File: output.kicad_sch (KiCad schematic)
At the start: 6 parts

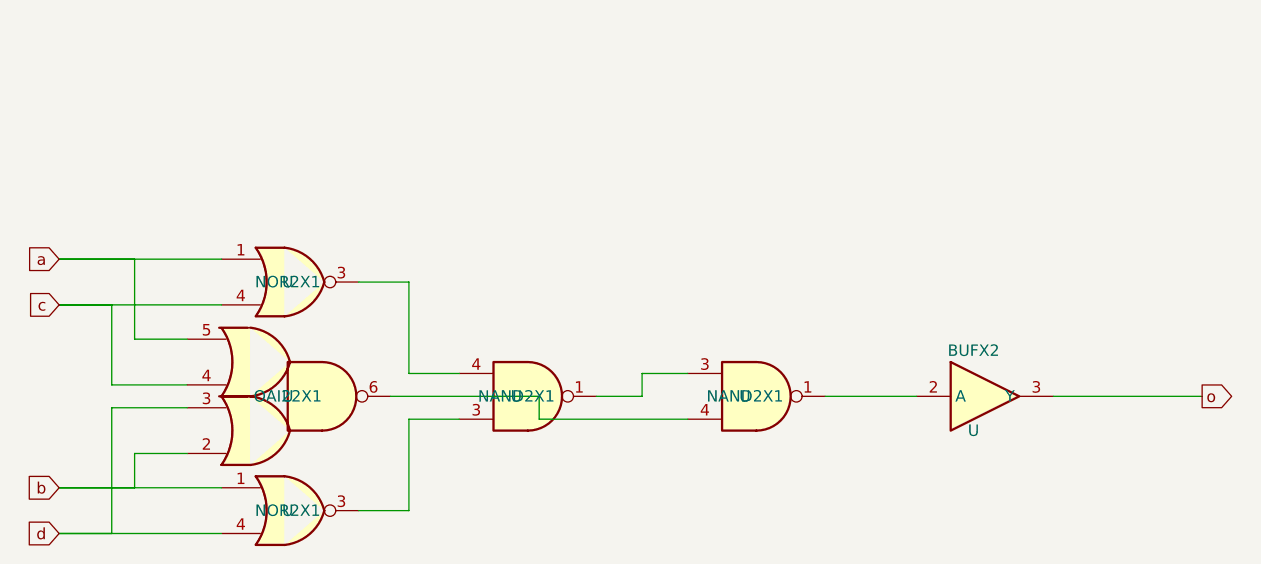
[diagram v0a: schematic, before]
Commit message: preserve and use pin names
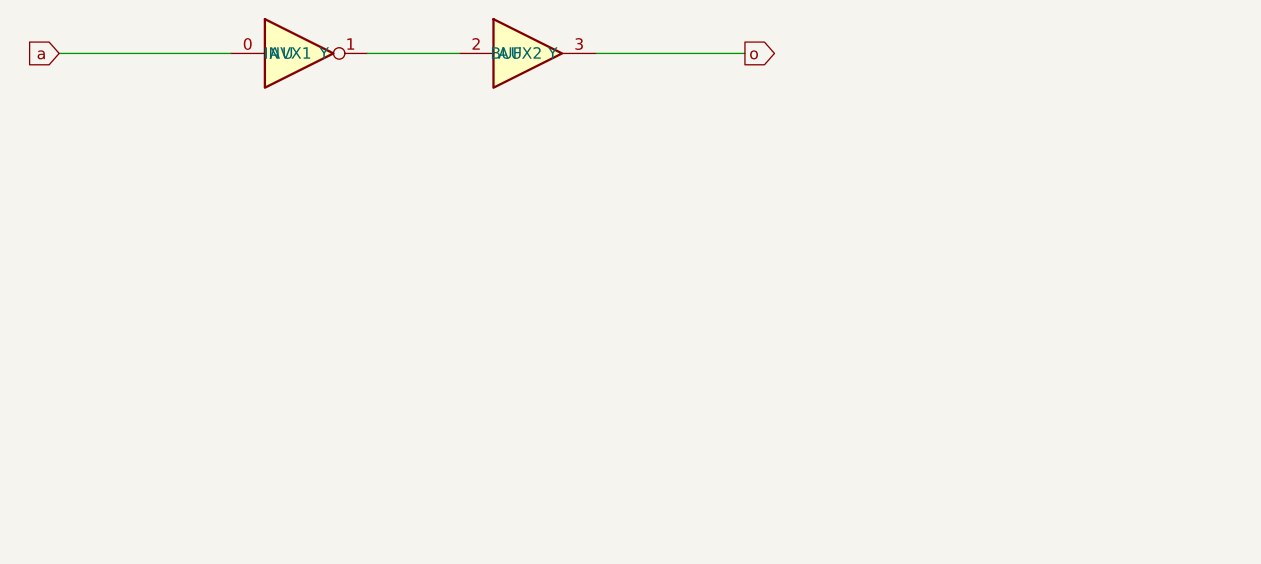
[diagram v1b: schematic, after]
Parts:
- removed U (x2): NOR2X1, symbol test:NOR2X1
- removed U (x2): NAND2X1, symbol test:NAND2X1
- removed U: OAI22X1, symbol test:OAI22X1
- added U: INVX1, symbol test:INVX1
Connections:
- net a: now also U.0 (A)
- net at U.2 (A): now also U.1 (Y)
